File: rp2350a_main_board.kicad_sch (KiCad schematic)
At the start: 75 parts, among them J1 USB_C_Receptacle_USB2.0_16P, J2 SM03B-SRSS-TB, J3 Micro_SD_Card_Det1, J4 SM03B-SRSS-TB, J5 Conn_02x12, J6 Conn_02x12, J7 Conn_02x12, J8 Conn_02x12, SW1 SW_SPDT, SW2 SW_Push, SW3 SW_Push, U1 TPS63802, U2 TPS2116DRL, U3 W25Q16JVSS, U4 RP2350_60QFN, U5 APS1604M-3SQRx-SN, Y1 ABM8-272-T3

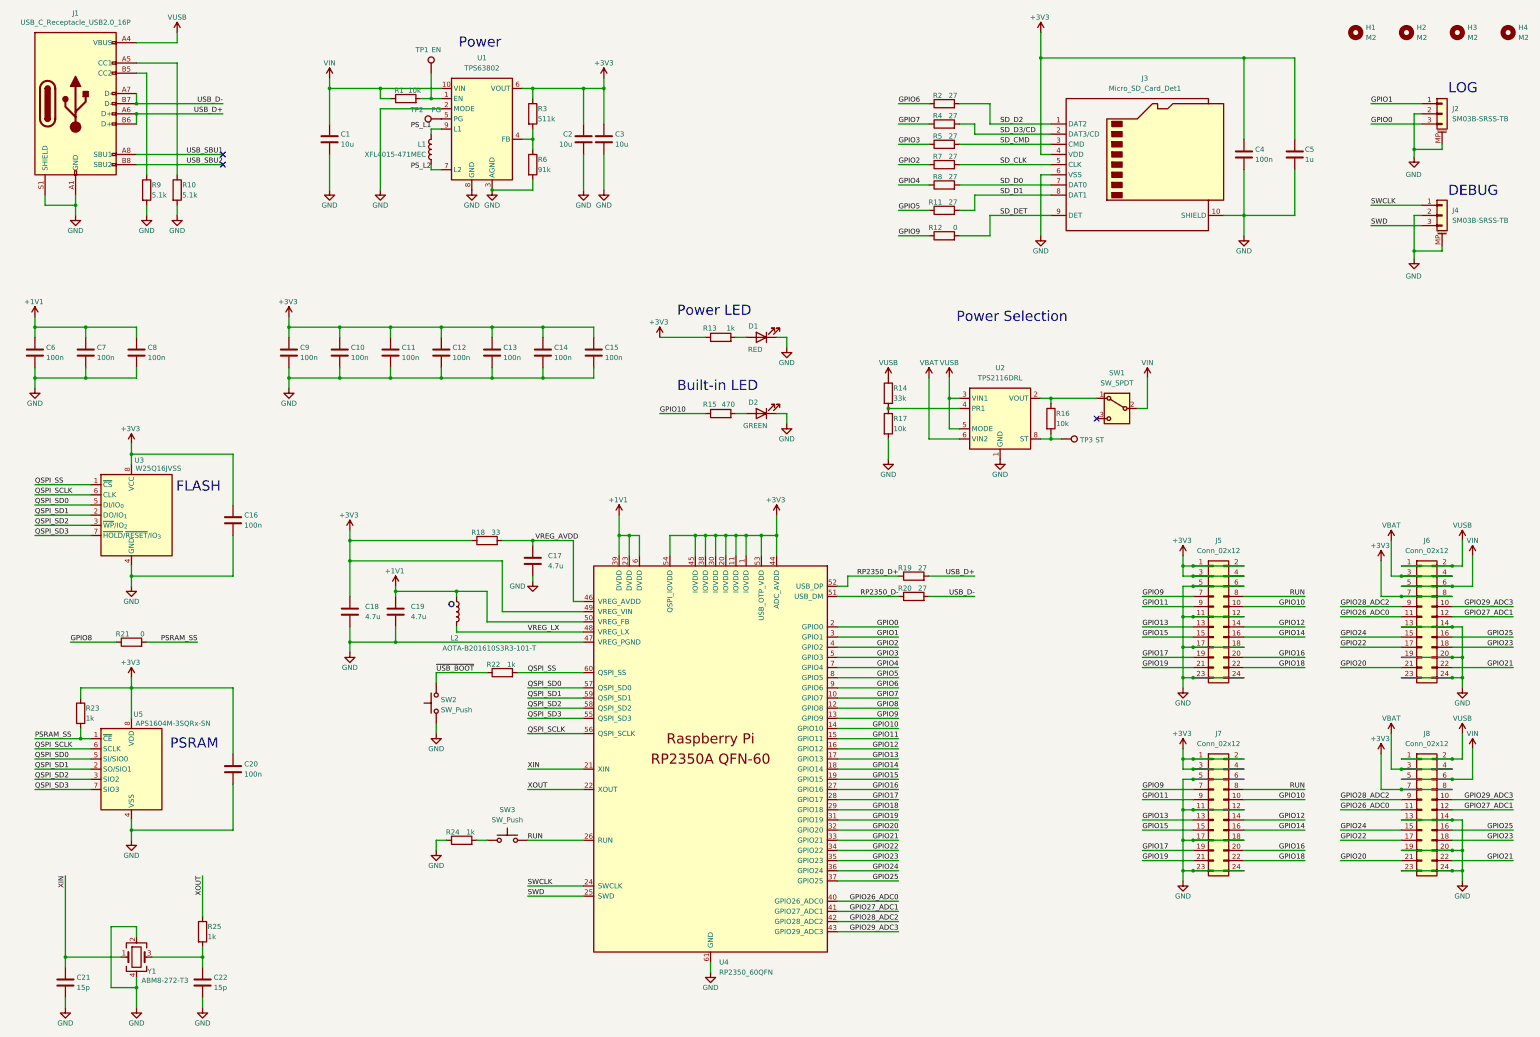
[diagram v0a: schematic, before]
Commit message: Switch to TPS2117 and update power circuit
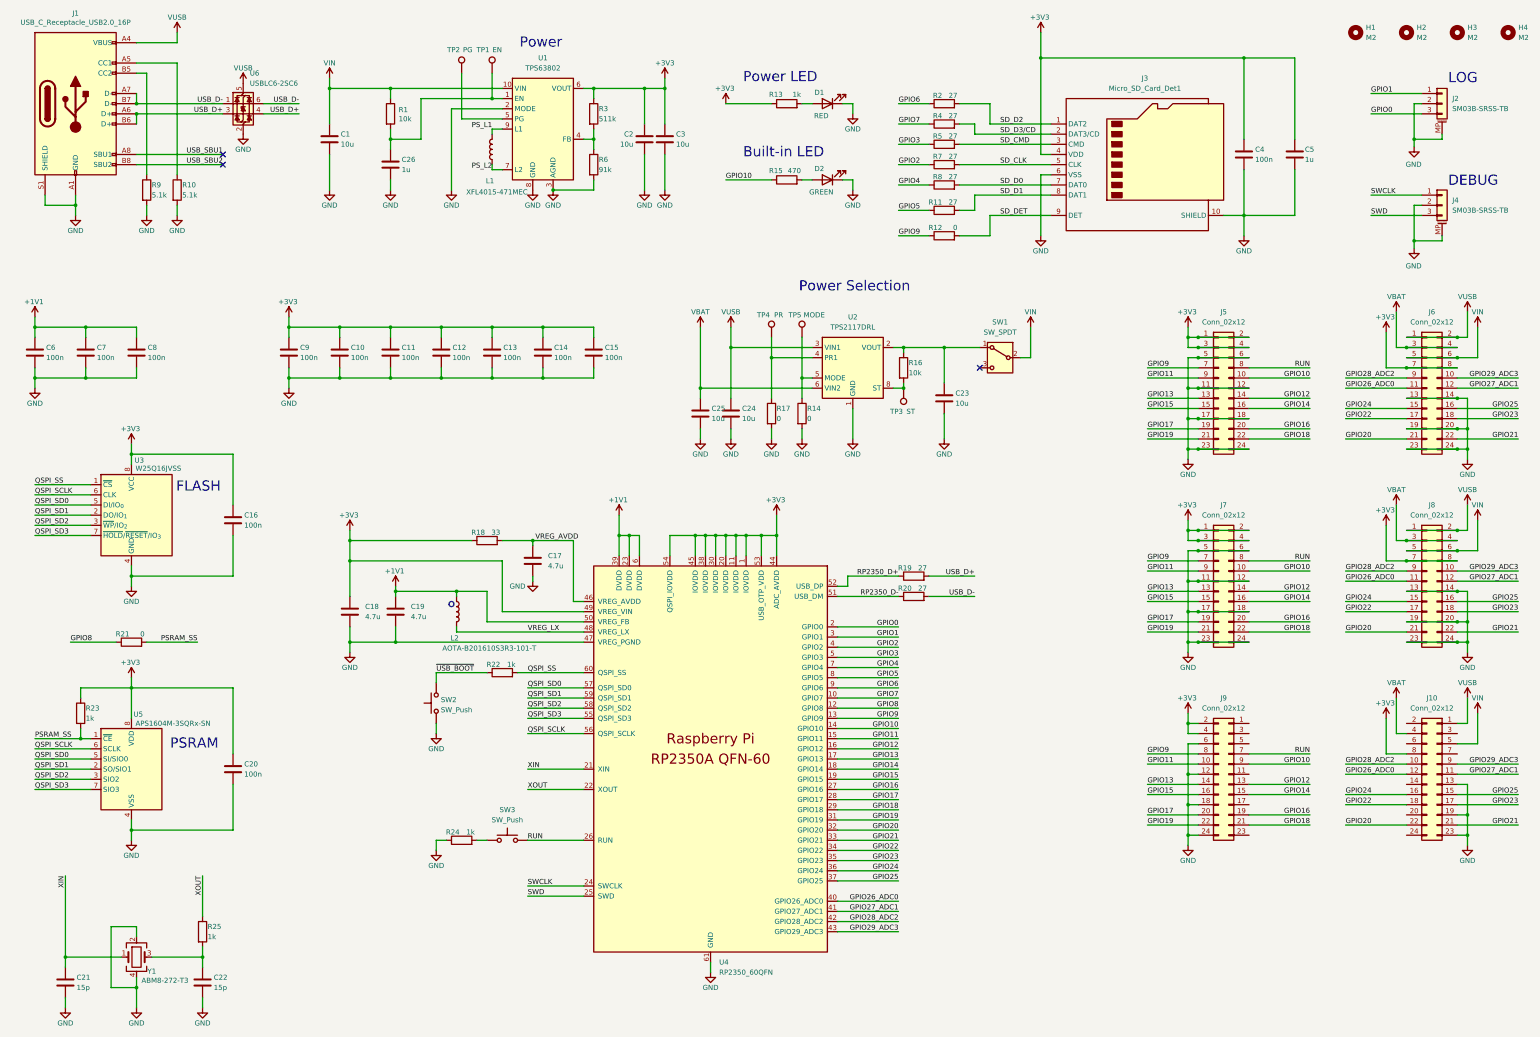
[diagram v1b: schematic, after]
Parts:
- added C23, C24, C25: 10u, Capacitor_SMD:C_0603_1608Metric_Pad1.08x0.95mm_HandSolder, symbol Device:C
- added C26: 1u, Capacitor_SMD:C_0402_1005Metric_Pad0.74x0.62mm_HandSolder, symbol Device:C
- added J10, J9: Conn_02x12, Connector_PinSocket_2.54mm:PinSocket_2x12_P2.54mm_Vertical_SMD, symbol Connector_Generic:Conn_02x12_Odd_Even
- added TP4: PR, TestPoint:TestPoint_Pad_D1.0mm, symbol Connector:TestPoint
- added TP5: MODE, TestPoint:TestPoint_Pad_D1.0mm, symbol Connector:TestPoint
- added U6: USBLC6-2SC6, Package_TO_SOT_SMD:SOT-23-6, symbol Power_Protection:USBLC6-2SC6
- R14: value 33k -> 0
- R17: value 10k -> 0
- U2: value TPS2116DRL -> TPS2117DRL
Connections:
- net +3V3: now also J10.8 (Pin_8), J9.2 (Pin_2), J9.4 (Pin_4)
- net GND: now also R14.2, C23.2, C24.2, C25.2, C26.2, J10.13 (Pin_13), J10.19 (Pin_19), J10.23 (Pin_23), J9.12 (Pin_12), J9.18 (Pin_18), J9.24 (Pin_24), J9.6 (Pin_6), U6.2 (GND)
- net GPIO10: now also J9.9 (Pin_9)
- net GPIO11: now also J9.10 (Pin_10)
- net GPIO12: now also J9.13 (Pin_13)
- net GPIO13: now also J9.14 (Pin_14)
- net GPIO14: now also J9.15 (Pin_15)
- net GPIO15: now also J9.16 (Pin_16)
- net GPIO16: now also J9.19 (Pin_19)
- net GPIO17: now also J9.20 (Pin_20)
- net GPIO18: now also J9.21 (Pin_21)
- net GPIO19: now also J9.22 (Pin_22)
- net GPIO20: now also J10.22 (Pin_22)
- net GPIO21: now also J10.21 (Pin_21)
- net GPIO22: now also J10.18 (Pin_18)
- net GPIO23: now also J10.17 (Pin_17)
- net GPIO24: now also J10.16 (Pin_16)
- net GPIO25: now also J10.15 (Pin_15)
- net GPIO26_ADC0: now also J10.12 (Pin_12)
- net GPIO27_ADC1: now also J10.11 (Pin_11)
- net GPIO28_ADC2: now also J10.10 (Pin_10)
- net GPIO29_ADC3: now also J10.9 (Pin_9)
- net GPIO9: now also J9.8 (Pin_8)
- net RUN: now also J9.7 (Pin_7)
- net USB_D+: now also U6.3 (I/O2), U6.4 (I/O2)
- net USB_D-: now also U6.1 (I/O1), U6.6 (I/O1)
- net VBAT: now also C25.1, J10.4 (Pin_4)
- net VIN: now also J10.5 (Pin_5)
- net VUSB: now also C24.1, J10.1 (Pin_1), U6.5 (VBUS); no longer R14.1, U2.5 (MODE)
- net at R1.2, TP1.1, U1.1 (EN): now also C26.1
- net at R16.1, SW1.1 (A), U2.2 (VOUT)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: now also C23.1
- net at R17.1, U2.4 (PR1): now also TP4.1; no longer R14.2
- new net: R14.1, TP5.1, U2.5 (MODE)
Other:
- moved on the sheet: C2, C3, D1, D2, J2, J4, J5, J6, J7, J8, L1, R1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

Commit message: v1.1.0 WIP
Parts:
- R15: footprint Resistor_SMD:R_0603_1608Metric_Pad0.98x0.95mm_HandSolder -> Resistor_SMD:R_0402_1005Metric_Pad0.72x0.64mm_HandSolder
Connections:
- net +3V3: now also J10.7 (Pin_7), J9.1 (Pin_1), J9.3 (Pin_3)
- net GND: now also J10.14 (Pin_14), J10.20 (Pin_20), J10.24 (Pin_24), J9.11 (Pin_11), J9.17 (Pin_17), J9.23 (Pin_23), J9.5 (Pin_5)
- net VBAT: now also J10.3 (Pin_3)
- net VIN: now also J10.6 (Pin_6)
- net VUSB: now also J10.2 (Pin_2)
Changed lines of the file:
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@@
 	)
 	(junction
+		(at 381 226.06)
+		(diameter 0)
+		(color 0 0 0 0)
+	)
+	(junction
 		(at 252.73 104.14)
 		(diameter 0)
@@
 	)
 	(junction
+		(at 381 203.2)
+		(diameter 0)
+		(color 0 0 0 0)
+	)
+	(junction
 		(at 199.39 104.14)
 		(diameter 0)
@@
 	)
 	(junction
+		(at 316.23 226.06)
+		(diameter 0)
+		(color 0 0 0 0)
+	)
+	(junction
 		(at 171.45 151.13)
 		(diameter 0)
@@
 	)
 	(junction
+		(at 316.23 200.66)
+		(diameter 0)
+		(color 0 0 0 0)
+	)
+	(junction
 		(at 381 129.54)
 		(diameter 0)
@@
 	)
 	(junction
+		(at 316.23 218.44)
+		(diameter 0)
+		(color 0 0 0 0)
+	)
+	(junction
 		(at 381 101.6)
 		(diameter 0)
@@
 	)
 	(junction
+		(at 368.3 200.66)
+		(diameter 0)
+		(color 0 0 0 0)
+	)
+	(junction
+		(at 381 198.12)
+		(diameter 0)
+		(color 0 0 0 0)
+	)
+	(junction
 		(at 101.6 111.76)
 		(diameter 0)
@@
 	)
 	(junction
+		(at 316.23 210.82)
+		(diameter 0)
+		(color 0 0 0 0)
+	)
+	(junction
 		(at 383.54 177.8)
 		(diameter 0)
@@
 	)
 	(junction
+		(at 381 220.98)
+		(diameter 0)
+		(color 0 0 0 0)
+	)
+	(junction
 		(at 49.53 224.79)
 		(diameter 0)
@@
 	)
 	(junction
+		(at 316.23 198.12)
+		(diameter 0)
+		(color 0 0 0 0)
+	)
+	(junction
 		(at 191.77 114.3)
 		(diameter 0)
@@
 	)
 	(junction
+		(at 316.23 203.2)
+		(diameter 0)
+		(color 0 0 0 0)
+	)
+	(junction
 		(at 49.53 161.29)
 		(diameter 0)
@@
 	)
 	(junction
+		(at 381 213.36)
+		(diameter 0)
+		(color 0 0 0 0)
+	)
+	(junction
 		(at 127 111.76)
 		(diameter 0)
@@
 		(color 0 0 0 0)
 	)
+	(junction
+		(at 368.3 205.74)
+		(diameter 0)
+		(color 0 0 0 0)
+	)
 	(no_connect
 		(at 72.39 58.42)
@@
 	(wire
 		(pts
+			(xy 368.3 205.74) (xy 381 205.74)
+		)
+		(stroke
+			(width 0)
+			(type default)
+		)
+	)
+	(wire
+		(pts
 			(xy 313.69 180.34) (xy 313.69 177.8)
 		)
@@
 	(wire
 		(pts
+			(xy 316.23 203.2) (xy 328.93 203.2)
+		)
+		(stroke
+			(width 0)
+			(type default)
+		)
+	)
+	(wire
+		(pts
 			(xy 313.69 149.86) (xy 316.23 149.86)
 		)
@@
 	(wire
 		(pts
+			(xy 368.3 213.36) (xy 381 213.36)
+		)
+		(stroke
+			(width 0)
+			(type default)
+		)
+	)
+	(wire
+		(pts
 			(xy 226.06 179.07) (xy 241.3 179.07)
 		)
@@
 	(wire
 		(pts
+			(xy 316.23 226.06) (xy 328.93 226.06)
+		)
+		(stroke
+			(width 0)
+			(type default)
+		)
+	)
+	(wire
+		(pts
 			(xy 313.69 101.6) (xy 316.23 101.6)
 		)
@@
 	(wire
 		(pts
+			(xy 368.3 200.66) (xy 381 200.66)
+		)
+		(stroke
+			(width 0)
+			(type default)
+		)
+	)
+	(wire
+		(pts
+			(xy 316.23 198.12) (xy 328.93 198.12)
+		)
+		(stroke
+			(width 0)
+			(type default)
+		)
+	)
+	(wire
+		(pts
 			(xy 316.23 205.74) (xy 303.53 205.74)
 		)
@@
 	(wire
 		(pts
+			(xy 368.3 203.2) (xy 381 203.2)
+		)
+		(stroke
+			(width 0)
+			(type default)
+		)
+	)
+	(wire
+		(pts
 			(xy 50.8 55.88) (xy 72.39 55.88)
 		)
@@
 	(wire
 		(pts
+			(xy 368.3 220.98) (xy 381 220.98)
+		)
+		(stroke
+			(width 0)
+			(type default)
+		)
+	)
+	(wire
+		(pts
 			(xy 316.23 223.52) (xy 303.53 223.52)
 		)
@@
 	(wire
 		(pts
+			(xy 316.23 210.82) (xy 328.93 210.82)
+		)
+		(stroke
+			(width 0)
+			(type default)
+		)
+	)
+	(wire
+		(pts
 			(xy 226.06 247.65) (xy 241.3 247.65)
 		)
@@
 	(wire
 		(pts
+			(xy 316.23 218.44) (xy 328.93 218.44)
+		)
+		(stroke
+			(width 0)
+			(type default)
+		)
+	)
+	(wire
+		(pts
 			(xy 50.8 269.24) (xy 50.8 264.16)
 		)
@@
 	(wire
 		(pts
+			(xy 316.23 200.66) (xy 328.93 200.66)
+		)
+		(stroke
+			(width 0)
+			(type default)
+		)
+	)
+	(wire
+		(pts
 			(xy 199.39 99.06) (xy 199.39 104.14)
 		)
@@
 	(wire
 		(pts
+			(xy 368.3 198.12) (xy 381 198.12)
+		)
+		(stroke
+			(width 0)
+			(type default)
+		)
+	)
+	(wire
+		(pts
 			(xy 256.54 58.42) (xy 279.4 58.42)
 		)
@@
 	(wire
 		(pts
+			(xy 368.3 226.06) (xy 381 226.06)
+		)
+		(stroke
+			(width 0)
+			(type default)
+		)
+	)
+	(wire
+		(pts
 			(xy 35.56 68.58) (xy 35.56 66.04)
 		)
@@
 			)
 		)
-		(property "Footprint" "Resistor_SMD:R_0603_1608Metric_Pad0.98x0.95mm_HandSolder"
+		(property "Footprint" "Resistor_SMD:R_0402_1005Metric_Pad0.72x0.64mm_HandSolder"
 			(at 213.36 64.008 90)
 			(effects

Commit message: Update BOM
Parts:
- J1: now in the parts list
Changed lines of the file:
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@@
 		(unit 1)
 		(exclude_from_sim no)
-		(in_bom no)
+		(in_bom yes)
 		(on_board yes)
 		(dnp no)
